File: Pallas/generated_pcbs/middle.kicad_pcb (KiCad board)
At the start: 2 copper layers, 467.5 x 140 mm, 260 parts, among them J1 OLED, J2 RGB_LED, Q1 IRLML6344TRPbF, SW00 SW_PUSH, SW01 SW_PUSH, SW010 SW_PUSH, SW011 SW_PUSH, SW012 SW_PUSH, SW013 SW_PUSH, SW014 SW_PUSH, SW02 SW_PUSH, SW03 SW_PUSH, SW04 SW_PUSH, SW05 SW_PUSH, SW06 SW_PUSH, SW07 SW_PUSH, SW08 SW_PUSH, SW09 SW_PUSH, SW10 SW_PUSH, SW11 SW_PUSH, SW110 SW_PUSH, SW111 SW_PUSH, SW112 SW_PUSH, SW113 SW_PUSH, SW114 SW_PUSH, SW12 SW_PUSH, SW13 SW_PUSH, SW14 SW_PUSH, SW15 SW_PUSH, SW16 SW_PUSH, SW17 SW_PUSH, SW18 SW_PUSH, SW19 SW_PUSH, SW20 SW_PUSH, SW21 SW_PUSH, SW210 SW_PUSH, SW211 SW_PUSH, SW212 SW_PUSH, SW213 SW_PUSH, SW214 SW_PUSH, SW22 SW_PUSH, SW23 SW_PUSH, SW24 SW_PUSH, SW25 SW_PUSH, SW26 SW_PUSH, SW27 SW_PUSH, SW28 SW_PUSH, SW29 SW_PUSH, SW30 SW_PUSH, SW31 SW_PUSH, SW310 SW_PUSH, SW311 SW_PUSH, SW312 SW_PUSH, SW313 SW_PUSH, SW314 SW_PUSH, SW32 SW_PUSH, SW33 SW_PUSH, SW34 SW_PUSH, SW35 SW_PUSH, SW36 SW_PUSH, SW37 SW_PUSH, SW38 SW_PUSH, SW39 SW_PUSH, SW40 SW_PUSH, SW41 SW_PUSH, SW410 SW_PUSH, SW411 SW_PUSH, SW412 SW_PUSH, SW413 SW_PUSH, SW414 SW_PUSH, SW42 SW_PUSH, SW43 SW_PUSH, SW44 SW_PUSH, SW45 SW_PUSH, SW46 SW_PUSH, SW47 SW_PUSH, SW48 SW_PUSH, SW49 SW_PUSH, U1 Elite-C

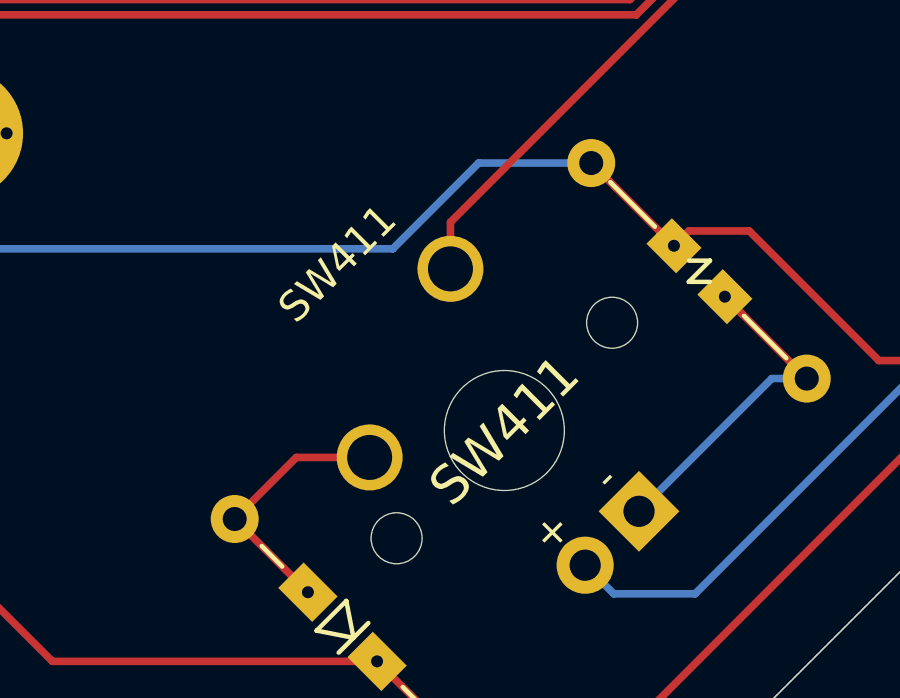
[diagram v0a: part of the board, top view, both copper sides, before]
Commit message: Consolidate symbol and fp libraries
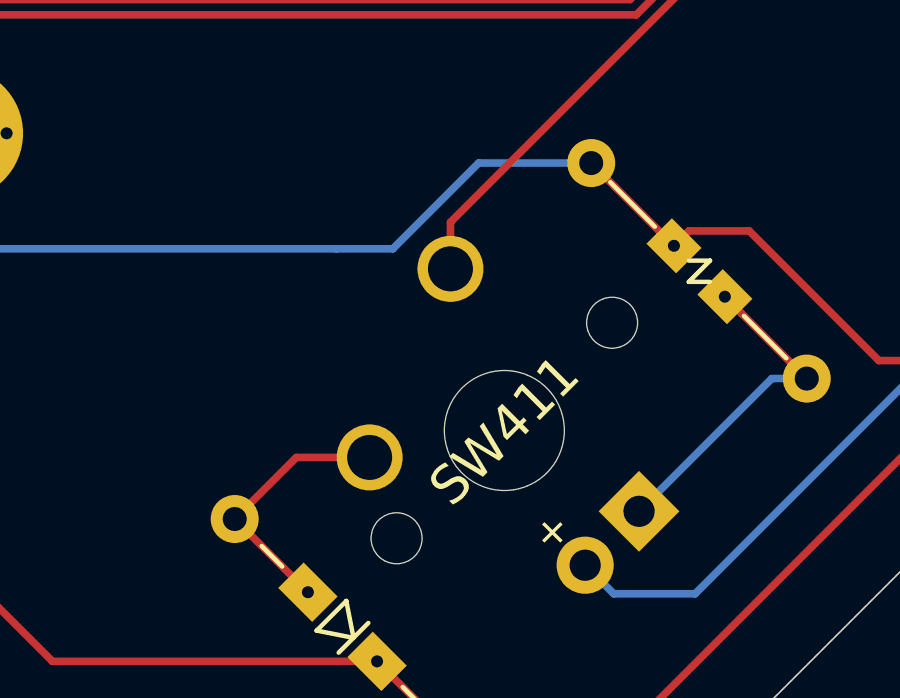
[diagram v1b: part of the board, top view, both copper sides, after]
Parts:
- removed the MountBaseMiddleTop15 at (526.4, 136.4)
- removed the MountBaseMiddleTop15 at (526.4, 43.9)
- added MountBaseMiddleTop15: MountingHole, Pallas:MountingHole_2.2mm_M2_Pad_Via, F.Cu at (526.4, 136.4)
- added MountBaseMiddleTop15: MountingHole, Pallas:MountingHole_2.2mm_M2_Pad_Via, F.Cu at (526.4, 43.9)
- D00, D01, D010, D011, D012, D013, D014, D02, D03, D04, D05, D06, D07, D08, D09, D10, D11, D110, D111, D112, D113, D114, D12, D13, D14, D15, D16, D17, D18, D19, D20, D21, D210, D211, D212, D213, D214, D22, D23, D24, D25, D26, D27, D28, D29, D30, D31, D310, D311, D312, D313, D314, D32, D33, D34, D35, D36, D37, D38, D39, D40, D41, D410, D411, D412, D413, D414, D42, D43, D44, D45, D46, D47, D48, D49: footprint keyboard:Diode_SMD_THT -> Pallas:Diode_SMD_THT
- J1: footprint keyboard:OLED_128x64_I2C -> Pallas:OLED_128x64_I2C
- J2: footprint keyboard:conn_3pins -> Pallas:conn_3pins
- LogoBaseMiddleTop: footprint keyboard:Ciaanh_signature -> Pallas:Ciaanh_signature
- LogoMiddle1, LogoMiddle2: footprint keyboard:athena -> Pallas:athena
- MountBaseMiddleTop0, MountBaseMiddleTop10, MountBaseMiddleTop11, MountBaseMiddleTop12, MountBaseMiddleTop13, MountBaseMiddleTop14, MountBaseMiddleTop2, MountBaseMiddleTop3, MountBaseMiddleTop4, MountBaseMiddleTop5, MountBaseMiddleTop6, MountBaseMiddleTop7, MountBaseMiddleTop8, MountBaseMiddleTop9: footprint keyboard:MountingHole_2.2mm_M2_Pad_Via -> Pallas:MountingHole_2.2mm_M2_Pad_Via
- MountForMiddle1, MountMiddle1, MountMiddle2, MountMiddle3: footprint keyboard:MountingHole_2.4mm_M2_Pad -> Pallas:MountingHole_2.4mm_M2_Pad
- Q1: footprint keyboard:SOT23-3_HSOL_Back -> Pallas:SOT23-3_HSOL_Back
- R00, R01, R010, R011, R012, R013, R014, R02, R03, R04, R05, R06, R07, R08, R09, R1, R10, R11, R110, R111, R112, R113, R114, R12, R13, R14, R15, R16, R17, R18, R19, R2, R20, R21, R210, R211, R212, R213, R214, R22, R23, R24, R25, R26, R27, R28, R29, R3, R30, R31, R310, R311, R312, R313, R314, R32, R33, R34, R35, R36, R37, R38, R39, R40, R41, R410, R411, R412, R413, R414, R42, R43, R44, R45, R46, R47, R48, R49: footprint keyboard:Resistors_SMD_THT -> Pallas:Resistors_SMD_THT
- RGB1, RGB2, RGB3, RGB4: footprint keyboard:WS2812B_Front -> Pallas:WS2812B_Front
- RSW0: footprint keyboard:SW_RST -> Pallas:SW_RST
- SW00, SW01, SW010, SW011, SW012, SW013, SW014, SW02, SW03, SW04, SW05, SW06, SW07, SW08, SW09, SW11, SW110, SW111, SW112, SW113, SW114, SW12, SW13, SW14, SW15, SW16, SW17, SW18, SW19, SW21, SW210, SW211, SW212, SW213, SW22, SW23, SW24, SW25, SW26, SW27, SW28, SW29, SW31, SW310, SW311, SW312, SW313, SW32, SW33, SW34, SW35, SW36, SW37, SW38, SW39, SW410, SW43, SW46, SW47, SW48, SW49: footprint keyboard:SW_Cherry_MX_1.00u_PCB -> Pallas:SW_Cherry_MX_1.00u_PCB
- SW10: footprint keyboard:SW_Cherry_MX_1.50u_PCB -> Pallas:SW_Cherry_MX_1.50u_PCB
- SW20, SW314: footprint keyboard:SW_Cherry_MX_1.75u_PCB -> Pallas:SW_Cherry_MX_1.75u_PCB
- SW214: footprint keyboard:SW_Cherry_MX_2.25u_ISO_PCB -> Pallas:SW_Cherry_MX_2.25u_ISO_PCB
- SW30: footprint keyboard:SW_Cherry_MX_2.25u_PCB -> Pallas:SW_Cherry_MX_2.25u_PCB
- SW40, SW41, SW411, SW413, SW414, SW42, SW45: footprint keyboard:SW_Cherry_MX_1.25u_PCB -> Pallas:SW_Cherry_MX_1.25u_PCB
- SW412: footprint keyboard:SW_Cherry_MX_2.75u_PCB -> Pallas:SW_Cherry_MX_2.75u_PCB
- SW44: footprint keyboard:SW_Cherry_MX_2.00u_PCB -> Pallas:SW_Cherry_MX_2.00u_PCB
- U1: footprint keyboard:Elite-C-castellated-29pin-holes -> Pallas:Elite-C-castellated-29pin-holes

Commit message: update pcb for footprint stabs
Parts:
- moved D214 1.28 mm to (503.1, 102.5)
- moved R214 1.25 mm to (517.6, 92.2)
- moved D30 1.19 mm to (84.0, 114.1)
- moved D44 1.12 mm to (187.6, 145.3)
- moved R30 1.11 mm to (98.5, 103.9)
- moved R44 1.10 mm to (203.9, 138.3)
- moved D412 0.92 mm to (382.7, 146.9)
- moved R412 0.91 mm to (395.1, 133.8)
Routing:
- net LED: track 2432.1 -> 2423.2 mm
- net row2: track 697.0 -> 698.3 mm
- net Net-(D44-Pad2): track 8.89 -> 7.69 mm
- net Net-(D30-Pad2): track 8.76 -> 7.58 mm
- net Net-(R44-Pad2): track 11.8 -> 10.6 mm
- net Net-(R30-Pad2): track 11.3 -> 10.2 mm
- net Net-(R412-Pad2): track 11.5 -> 10.5 mm
- net Net-(D214-Pad2): track 33.4 -> 32.6 mm
- net Net-(D412-Pad2): track 8.77 -> 8.18 mm

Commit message: rev 0.2 fix diode an res position with stabs
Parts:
- moved R214 21.1 mm to (523.1, 112.7), turned to 90 degrees
- moved D44 19.0 mm to (202.8, 133.8), turned to 168 degrees
- moved D30 18.8 mm to (96.2, 99.8), turned to 180 degrees
- moved R30 17.7 mm to (86.2, 116.6), turned to 0 degrees
- moved R44 17.7 mm to (189.2, 148.1), turned to 348 degrees
- moved D214 13.6 mm to (491.6, 95.2)
- moved R412 9.84 mm to (404.8, 131.8)
- moved D412 9.81 mm to (372.9, 147.3)
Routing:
- net LED: track 2423.2 -> 2375.6 mm
- net row3: track 614.6 -> 600.4 mm, vias 28 -> 24
- net Net-(R412-Pad2): track 10.5 -> 21.6 mm
- net row2: track 698.3 -> 687.7 mm, vias 28 -> 26
- net row4: track 622.8 -> 633.2 mm, vias 0 -> 2
- net Net-(D412-Pad2): track 8.18 -> 17.8 mm
- net Net-(D214-Pad2): track 32.6 -> 41.7 mm
- net Net-(R214-Pad2): track 16.4 -> 23.1 mm
- net col14: track 352.9 -> 359.3 mm, vias 2 -> 0
- net col0: track 279.2 -> 283.7 mm, vias 0 -> 2
- net Net-(R44-Pad2): track 10.6 -> 7.64 mm
- net Net-(R30-Pad2): track 10.2 -> 7.24 mm
- net VCC: track 2294.1 -> 2291.1 mm
- net col5: track 214.1 -> 211.3 mm, vias 0 -> 4
- net Net-(D30-Pad2): track 7.58 -> 10.1 mm
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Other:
- board text added: "Pallas rev 0.2 *prototype*"
- board text removed: "Pallas rev 0.1 *prototype*"
